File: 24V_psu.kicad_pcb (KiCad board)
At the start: 2 copper layers, 92.5 x 45 mm, 26 parts, among them J1 AC_IN, J2 DC_OUT, Q1 TIP122, Q2 BC546B

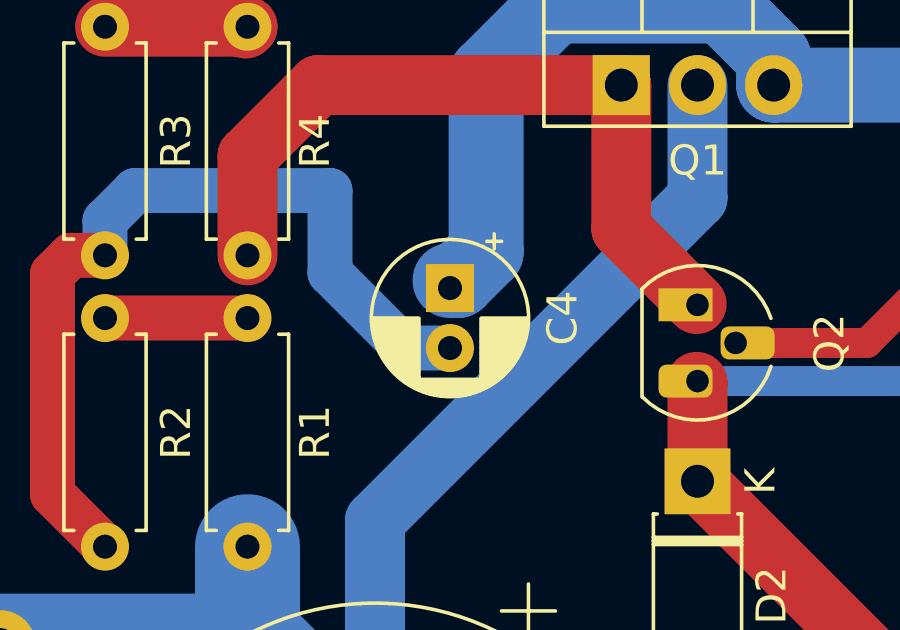
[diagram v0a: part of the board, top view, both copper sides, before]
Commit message: Change C4 footprint to non-polarized
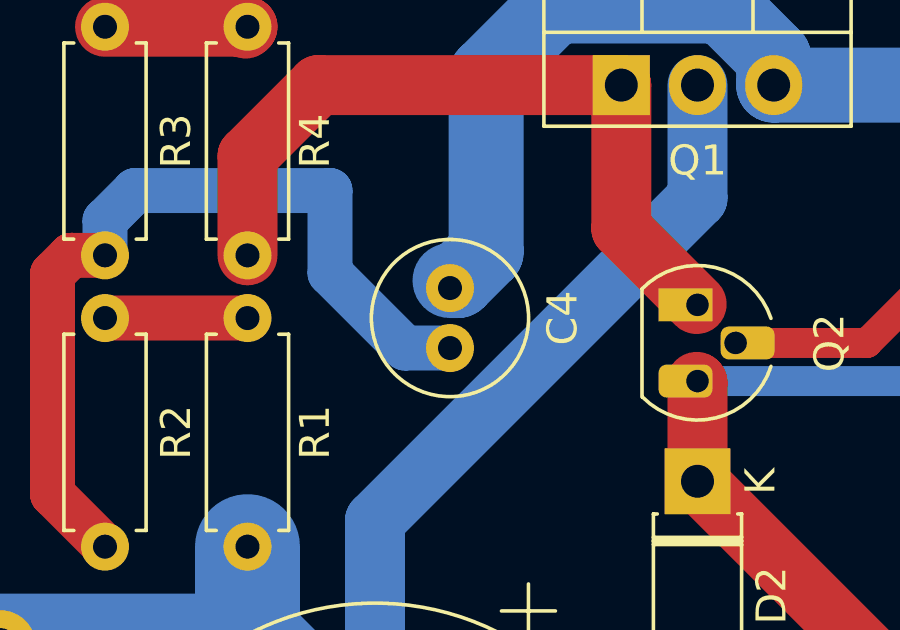
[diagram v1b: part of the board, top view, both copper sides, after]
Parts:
- C4: footprint Capacitor_THT:CP_Radial_D5.0mm_P2.00mm -> Capacitor_THT:C_Radial_D5.0mm_H11.0mm_P2.00mm

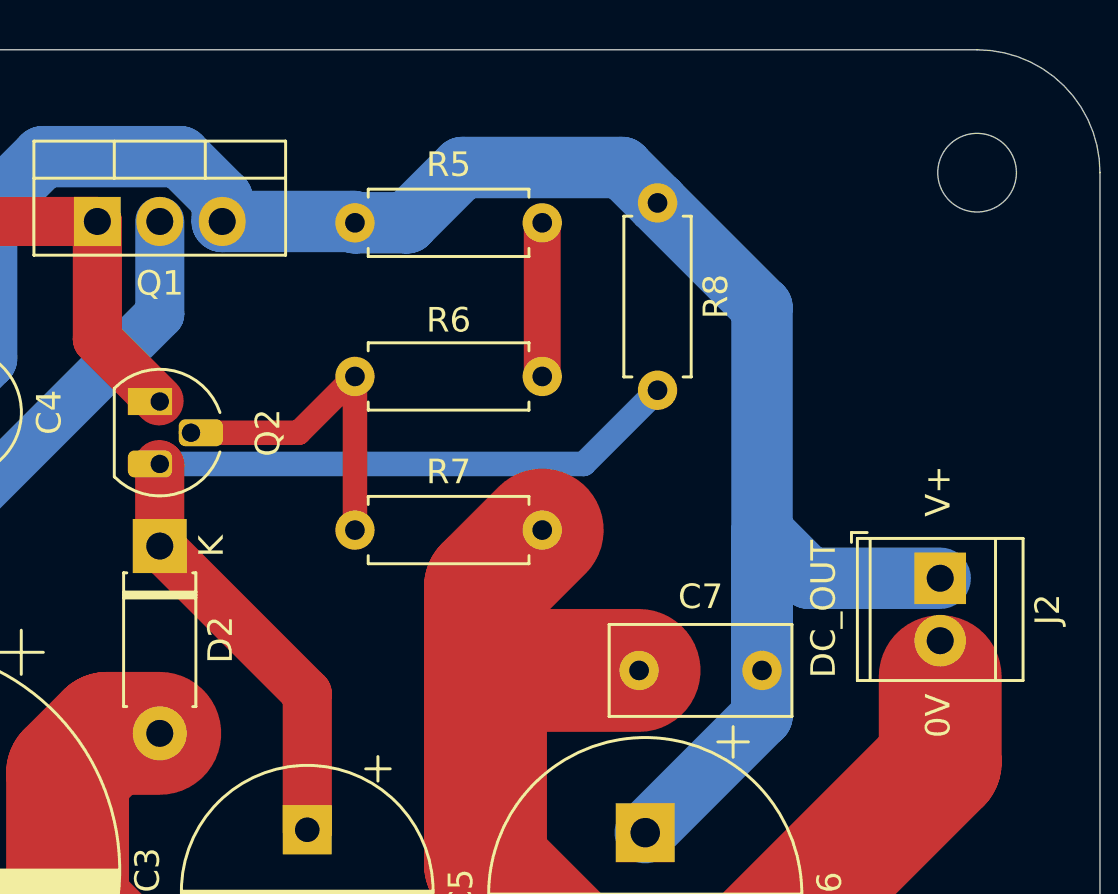
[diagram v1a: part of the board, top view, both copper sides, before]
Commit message: Move R5, R6 and R8 to provide space for a heatsink
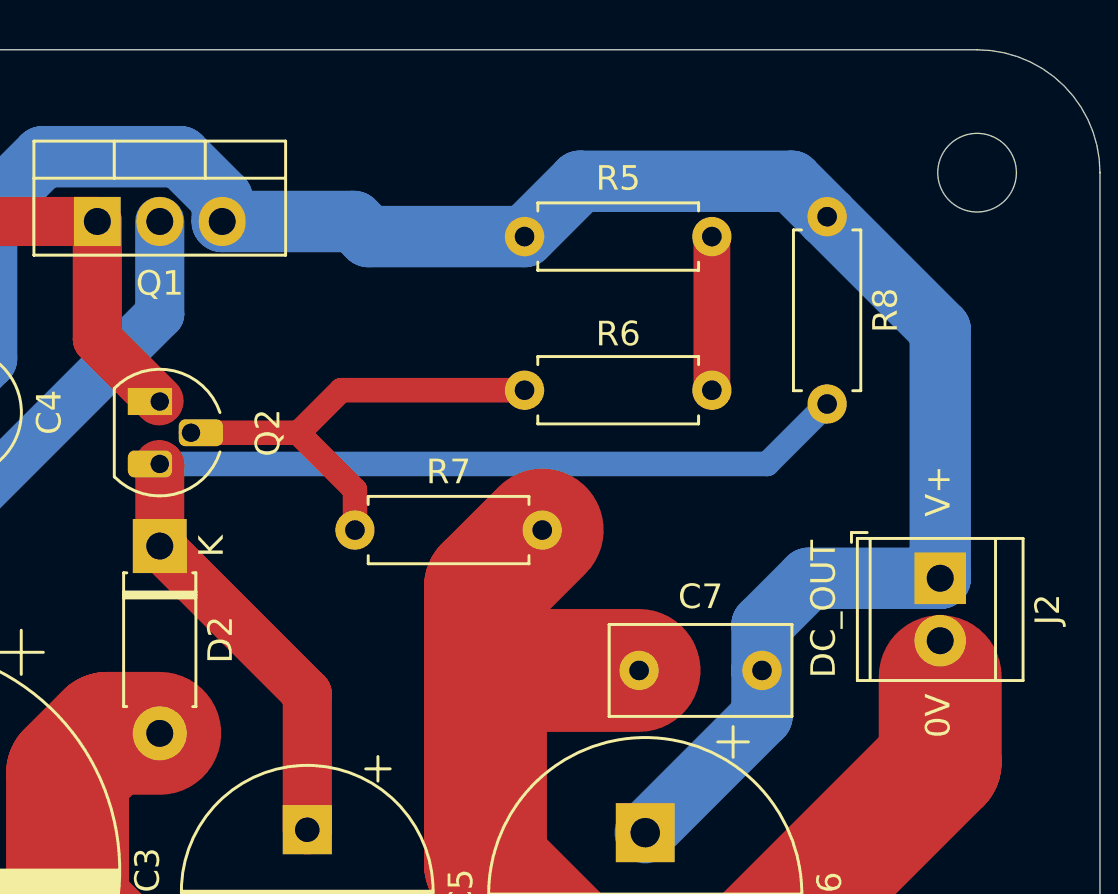
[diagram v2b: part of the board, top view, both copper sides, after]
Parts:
- moved R5 6.92 mm to (216.6, 55.1)
- moved R6 6.92 mm to (224.2, 61.4)
- moved R8 6.92 mm to (228.9, 54.3)
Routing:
- net Net-(D2-K): track 38.8 -> 45.5 mm
- net Net-(Q2-B): track 13.9 -> 19.2 mm
- net V_OUT: track 83.6 -> 81.1 mm
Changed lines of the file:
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@@
 	(footprint "Resistor_THT:R_Axial_DIN0207_L6.3mm_D2.5mm_P7.62mm_Horizontal"
 		(layer "F.Cu")
-		(at 217.31 60.79 180)
+		(at 224.21 61.35 180)
 		(descr "Resistor, Axial_DIN0207 series, Axial, Horizontal, pin pitch=7.62mm, 0.25W = 1/4W, length*diameter=6.3*2.5mm^2, http://cdn-reichelt.de/documents/datenblatt/B400/1_4W%23YAG.pdf")
 		(tags "Resistor Axial_DIN0207 series Axial Horizontal pin pitch 7.62mm 0.25W = 1/4W length 6.3mm diameter 2.5mm")
@@
 	(footprint "Resistor_THT:R_Axial_DIN0207_L6.3mm_D2.5mm_P7.62mm_Horizontal"
 		(layer "F.Cu")
-		(at 222 53.73 -90)
+		(at 228.9 54.29 -90)
 		(descr "Resistor, Axial_DIN0207 series, Axial, Horizontal, pin pitch=7.62mm, 0.25W = 1/4W, length*diameter=6.3*2.5mm^2, http://cdn-reichelt.de/documents/datenblatt/B400/1_4W%23YAG.pdf")
 		(tags "Resistor Axial_DIN0207 series Axial Horizontal pin pitch 7.62mm 0.25W = 1/4W length 6.3mm diameter 2.5mm")
@@
 	(footprint "Resistor_THT:R_Axial_DIN0207_L6.3mm_D2.5mm_P7.62mm_Horizontal"
 		(layer "F.Cu")
-		(at 209.69 54.54)
+		(at 216.59 55.1)
 		(descr "Resistor, Axial_DIN0207 series, Axial, Horizontal, pin pitch=7.62mm, 0.25W = 1/4W, length*diameter=6.3*2.5mm^2, http://cdn-reichelt.de/documents/datenblatt/B400/1_4W%23YAG.pdf")
 		(tags "Resistor Axial_DIN0207 series Axial Horizontal pin pitch 7.62mm 0.25W = 1/4W length 6.3mm diameter 2.5mm")
@@
 	)
 	(segment
-		(start 211.81 54.54)
-		(end 214.06 52.29)
+		(start 194.705113 54.137387)
+		(end 194.705113 60.044887)
 		(width 2.5)
 		(layer "B.Cu")
@@
 	)
 	(segment
-		(start 194.705113 54.137387)
-		(end 194.705113 60.044887)
+		(start 226.25 70.9)
+		(end 226.25 72.75)
 		(width 2.5)
 		(layer "B.Cu")
@@
 	)
 	(segment
-		(start 209.635 54.485)
-		(end 209.69 54.54)
+		(start 228.9 54.29)
+		(end 233.5 58.89)
 		(width 2.5)
 		(layer "B.Cu")
@@
 	)
 	(segment
-		(start 204.29 54.485)
+		(start 210.25 55.1)
 		(end 209.635 54.485)
 		(width 2.5)
@@
 	)
 	(segment
+		(start 226.25 72.75)
+		(end 226.25 74.6)
+		(width 2.5)
+		(layer "B.Cu")
+		(net 6)
+	)
+	(segment
+		(start 216.59 55.1)
+		(end 210.25 55.1)
+		(width 2.5)
+		(layer "B.Cu")
+		(net 6)
+	)
+	(segment
 		(start 228.15 69)
 		(end 233.5 69)
@@
 	)
 	(segment
-		(start 220.56 52.29)
-		(end 222 53.73)
-		(width 2.5)
-		(layer "B.Cu")
-		(net 6)
-	)
-	(segment
-		(start 222 53.73)
-		(end 226.25 57.98)
+		(start 228.15 69)
+		(end 226.25 70.9)
 		(width 2.5)
 		(layer "B.Cu")
@@
 	)
 	(segment
-		(start 202.579823 51.85)
-		(end 196.9925 51.85)
+		(start 209.635 54.485)
+		(end 204.29 54.485)
 		(width 2.5)
 		(layer "B.Cu")
@@
 	)
 	(segment
-		(start 209.69 54.54)
-		(end 211.81 54.54)
+		(start 227.459 52.849)
+		(end 228.9 54.29)
 		(width 2.5)
 		(layer "B.Cu")
@@
 	)
 	(segment
-		(start 226.25 67.1)
-		(end 226.25 74.6)
+		(start 216.59 55.1)
+		(end 218.841 52.849)
 		(width 2.5)
 		(layer "B.Cu")
@@
 	)
 	(segment
-		(start 226.25 67.1)
-		(end 228.15 69)
+		(start 202.579823 51.85)
+		(end 196.9925 51.85)
 		(width 2.5)
 		(layer "B.Cu")
@@
 	)
 	(segment
-		(start 214.06 52.29)
-		(end 220.56 52.29)
+		(start 218.841 52.849)
+		(end 227.459 52.849)
 		(width 2.5)
 		(layer "B.Cu")
@@
 	)
 	(segment
-		(start 226.25 67.1)
-		(end 226.25 74.35)
-		(width 2.5)
-		(layer "B.Cu")
-		(net 6)
-	)
-	(segment
-		(start 226.25 57.98)
-		(end 226.25 67.1)
+		(start 233.5 58.89)
+		(end 233.5 69)
 		(width 2.5)
 		(layer "B.Cu")
@@
 	)
 	(segment
-		(start 219 64.35)
-		(end 222 61.35)
+		(start 226.46 64.35)
+		(end 228.9 61.91)
 		(width 1)
 		(layer "B.Cu")
@@
 	(segment
 		(start 201.75 64.35)
-		(end 219 64.35)
+		(end 226.46 64.35)
 		(width 1)
 		(layer "B.Cu")
@@
 	)
 	(segment
+		(start 209.69 65.4)
+		(end 209.69 67.04)
+		(width 1)
+		(layer "F.Cu")
+		(net 9)
+	)
+	(segment
+		(start 209.13 61.35)
+		(end 207.4 63.08)
+		(width 1)
+		(layer "F.Cu")
+		(net 9)
+	)
+	(segment
 		(start 207.4 63.08)
 		(end 203.02 63.08)
@@
 	)
 	(segment
-		(start 209.69 60.79)
-		(end 209.69 67.04)
+		(start 207.4 63.11)
+		(end 209.69 65.4)
+		(width 1)
+		(layer "F.Cu")
+		(net 9)
+	)
+	(segment
+		(start 216.59 61.35)
+		(end 209.13 61.35)
 		(width 1)
 		(layer "F.Cu")
@@
 	(segment
 		(start 207.4 63.08)
-		(end 209.69 60.79)
+		(end 207.4 63.11)
 		(width 1)
 		(layer "F.Cu")
@@
 	)
 	(segment
-		(start 217.31 54.54)
-		(end 217.31 60.79)
+		(start 224.21 55.1)
+		(end 224.21 61.35)
 		(width 1.5)
 		(layer "F.Cu")

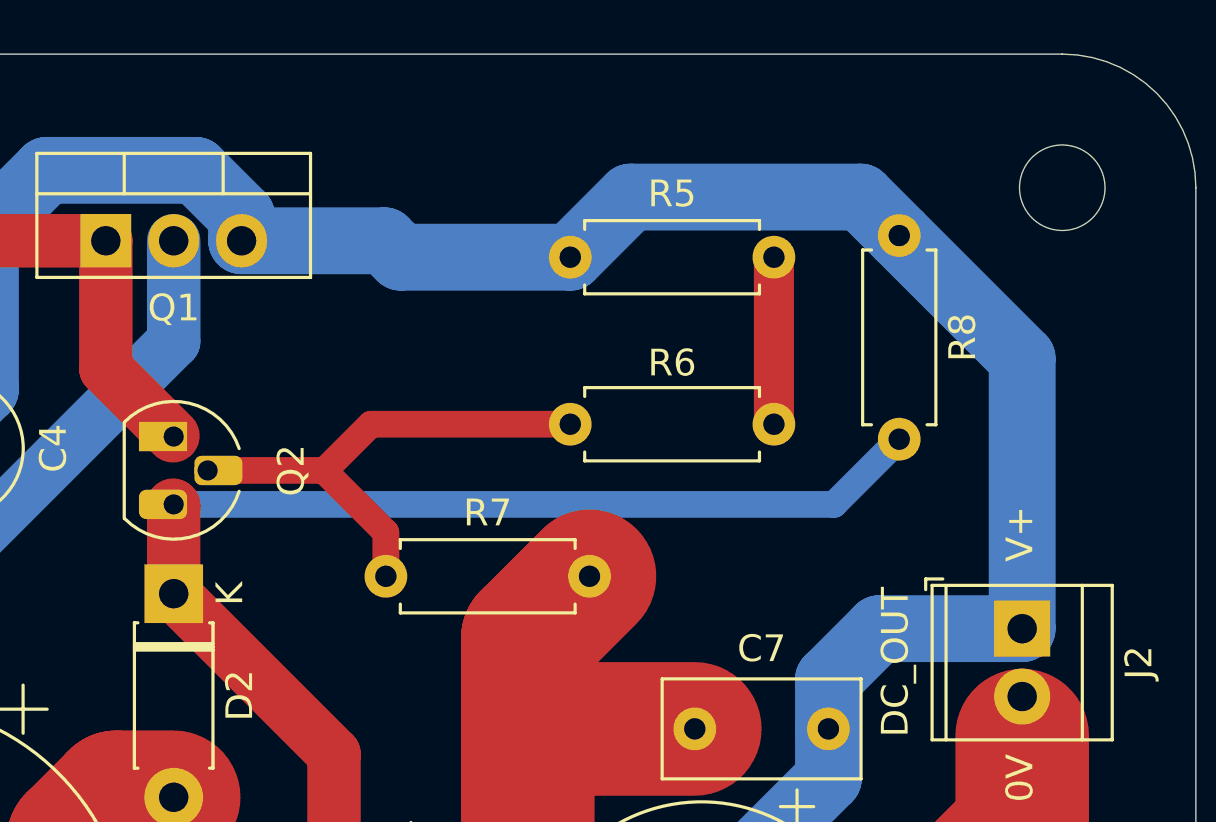
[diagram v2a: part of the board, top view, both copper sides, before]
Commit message: Add C8 for slightly improved ripple rejection
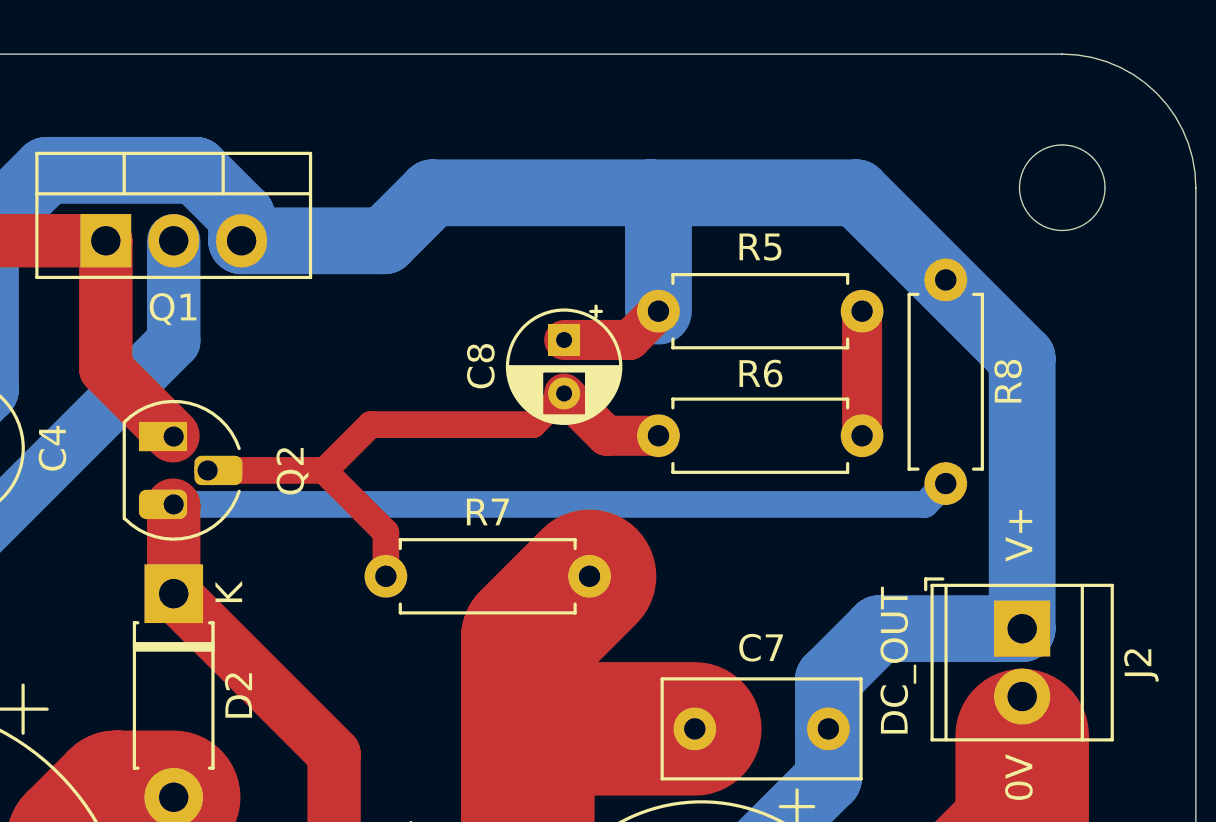
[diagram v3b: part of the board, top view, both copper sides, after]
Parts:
- added C8: 4u7, Capacitor_THT:CP_Radial_D4.0mm_P2.00mm, F.Cu at (216.4, 58.2)
- moved R5 3.87 mm to (219.9, 57.1)
- moved R6 3.33 mm to (227.5, 61.8)
- moved R8 2.40 mm to (230.6, 56.0)
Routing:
- net V_OUT: track 81.1 -> 89.3 mm
- net Net-(Q2-B): track 19.2 -> 23.6 mm
- net Net-(R5-Pad2): track 6.25 -> 4.66 mm
- net Net-(D2-K): track 45.5 -> 46.6 mm

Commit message: Change J1 and J2 to 5mm pitch
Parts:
- J1, J2: footprint TerminalBlock_TE-Connectivity:TerminalBlock_TE_282834-2_1x02_P2.54mm_Horizontal -> TerminalBlock:TerminalBlock_MaiXu_MX126-5.0-02P_1x02_P5.00mm
- moved J1 0.76 mm to (159.0, 62.5)
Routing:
- net AC_1: track 20.0 -> 20.6 mm
